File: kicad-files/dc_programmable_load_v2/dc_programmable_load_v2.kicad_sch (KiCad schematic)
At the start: 43 parts, among them J1 DC Jack 12V, J3 Conn_01x04_Socket, Q1 IRF3205, U1 LM358DR, U2 ER_OLEDM0.91_1x-I2C, U3 AP63200WU, U4 DS18B20

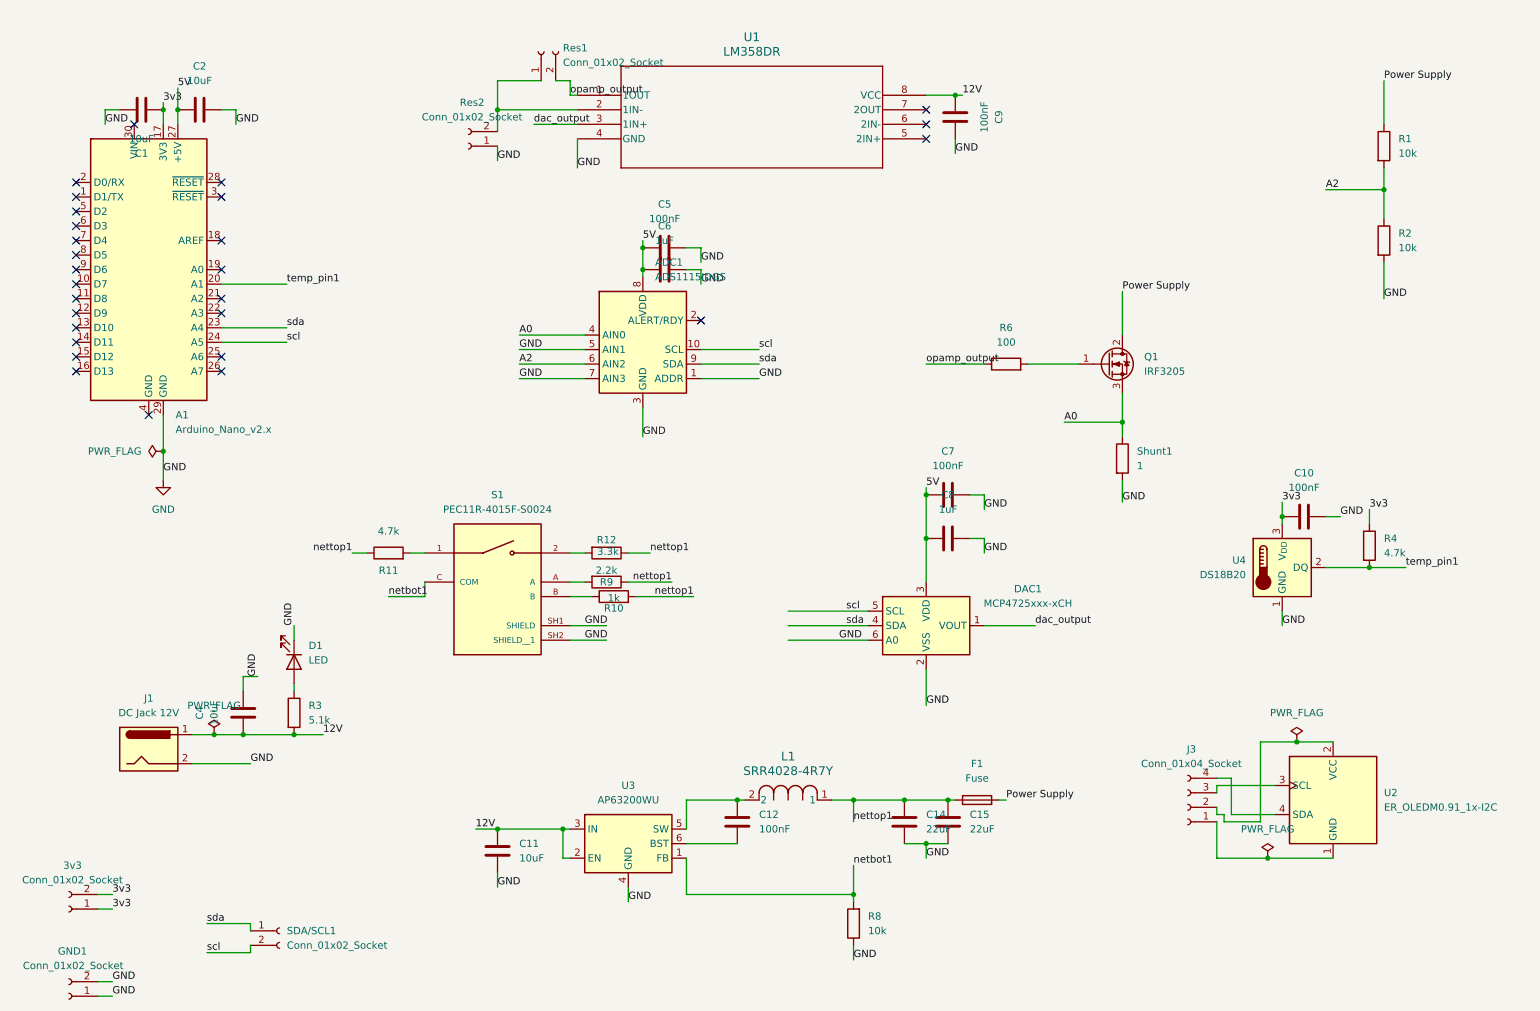
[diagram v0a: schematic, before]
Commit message: Update v2 schematic and PCB layout
Co-Authored-By: Claude Opus 5 (1M context) <noreply@anthropic.com>
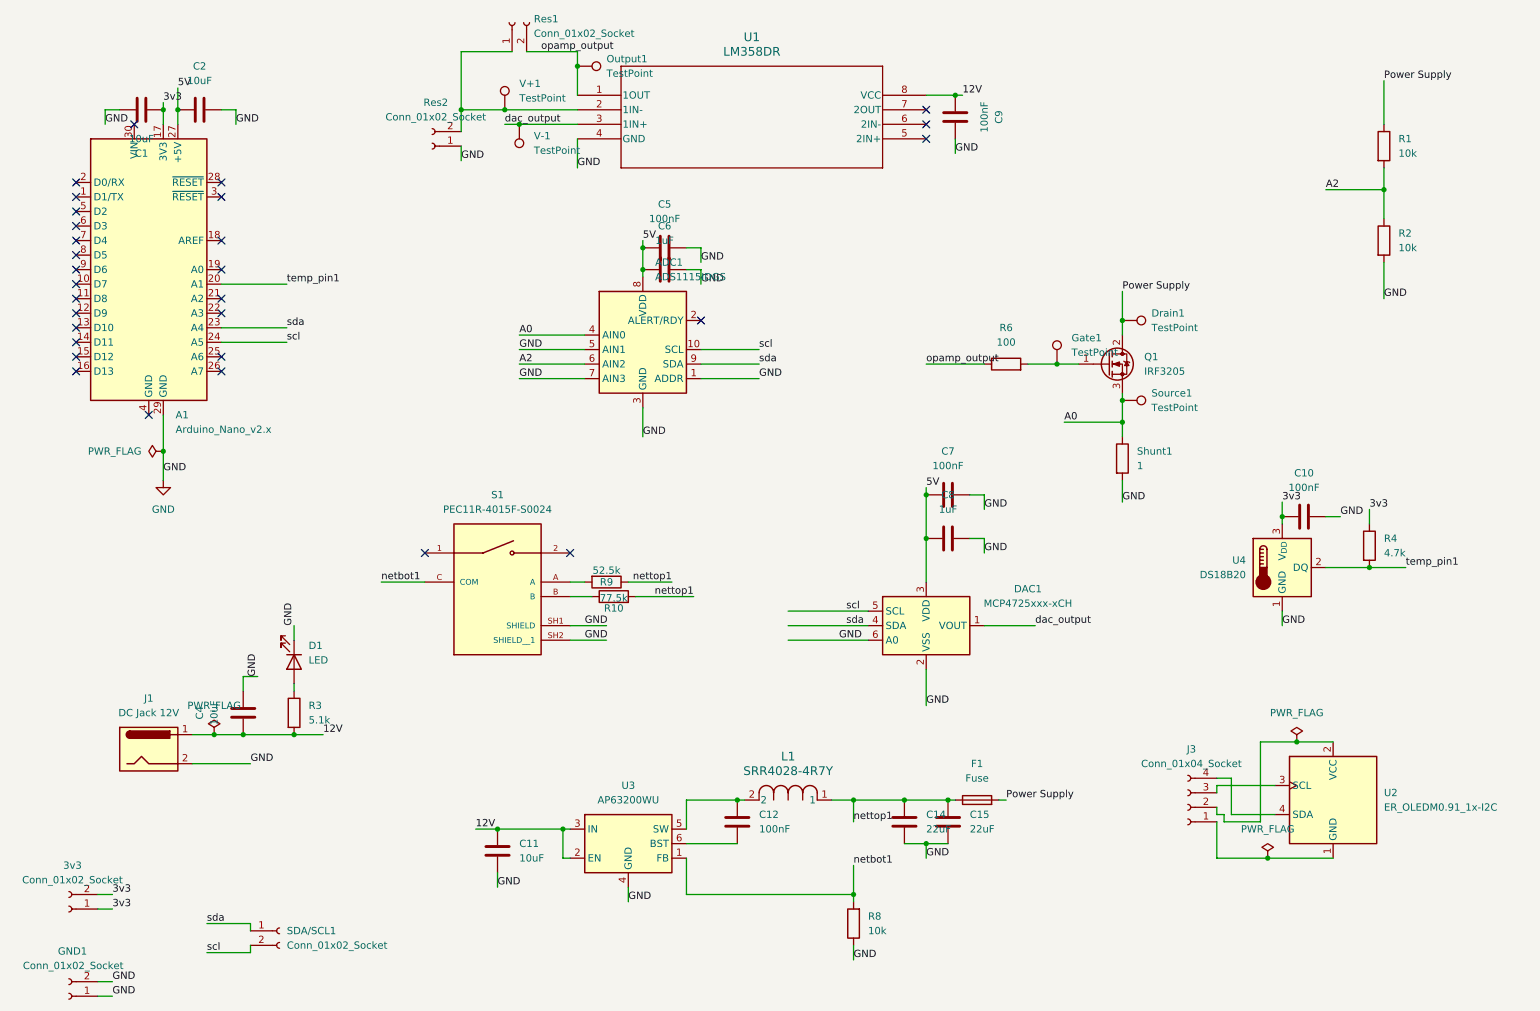
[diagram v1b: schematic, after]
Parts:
- removed R11: 4.7k, Resistor_SMD:R_0805_2012Metric, symbol Device:R
- removed R12: 3.3k, Resistor_SMD:R_0805_2012Metric, symbol Device:R
- added Drain1, Gate1, Output1, Source1, V+1, V-1: TestPoint, TestPoint:TestPoint_Keystone_5010-5014_Multipurpose, symbol Connector:TestPoint
- R10: value 1k -> 77.5k
- R9: value 2.2k -> 52.5k
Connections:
- net A0: now also Source1.1
- net Power Supply: now also Drain1.1
- net dac_output: now also V-1.1
- net opamp_output: now also Output1.1
- net at Q1.1 (G), R6.2: now also Gate1.1
- net at Res1.1 (Pin_1), Res2.2 (Pin_2), U1.2 (1IN-): now also V+1.1
- no-connect marks 28 -> 30
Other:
- moved on the sheet: Res1, Res2
